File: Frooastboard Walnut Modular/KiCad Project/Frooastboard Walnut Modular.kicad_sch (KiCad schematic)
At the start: 89 parts, among them J1 SW Interface, J2 Conn_01x16, J3 Conn_01x06, J4 Conn_01x06, J5 Conn_01x10, J6 Conn_01x12, J7 Conn_01x04, U1 RP2040, U2 SPX3819M5-L-3-3, U3 W25Q32JVZP, U4 nRF8001, U5 IS31FL3733-QF, U6 FS312F-G, U7 FS8205, U8 IP2312, Y1 32.768kHz, Y2 16MHz, Y3 12MHz

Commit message: some backup
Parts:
- BT1: footprint TestPoint:TestPoint_Pad_D1.5mm -> TestPoint:TestPoint_2Pads_Pitch5.08mm_Drill1.3mm
- J1: footprint Connector_PinHeader_2.54mm:PinHeader_1x05_P2.54mm_Vertical -> Connector_PinHeader_1.27mm:PinHeader_1x05_P1.27mm_Vertical
- TP5: footprint TestPoint:TestPoint_Pad_D1.5mm -> Connector_PinHeader_1.27mm:PinHeader_1x02_P1.27mm_Vertical
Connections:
- net RP_RESET: now also R8.2, U1.26 (~{RUN})
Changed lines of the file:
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@@
   (junction (at 255.27 182.88) (diameter 0) (color 0 0 0 0)
   )
+  (junction (at 30.48 34.29) (diameter 0) (color 0 0 0 0)
+  )
   (junction (at 309.245 184.15) (diameter 0) (color 0 0 0 0)
   )
@@
     (stroke (width 0) (type default) (color 0 0 0 0))
   )
+  (wire (pts (xy 27.94 34.29) (xy 30.48 34.29))
+    (stroke (width 0) (type default) (color 0 0 0 0))
+  )
   (wire (pts (xy 370.84 107.95) (xy 370.84 110.49))
     (stroke (width 0) (type default) (color 0 0 0 0))
@@
     )
   )
+  (global_label "RP_RESET" (shape input) (at 27.94 34.29 180) (fields_autoplaced)
+    (effects (font (size 1.27 1.27)) (justify right))
+    (property "Intersheet References" "${INTERSHEET_REFS}" (id 0) (at 16.274 34.2106 0)
+      (effects (font (size 1.27 1.27)) (justify right) hide)
+    )
+  )
   (global_label "NRF_REQN" (shape input) (at 76.2 90.17 0) (fields_autoplaced)
     (effects (font (size 1.27 1.27)) (justify left))
@@
       (effects (font (size 1.27 1.27)) (justify left))
     )
-    (property "Footprint" "TestPoint:TestPoint_Pad_D1.5mm" (id 2) (at 294.64 84.836 90)
+    (property "Footprint" "TestPoint:TestPoint_2Pads_Pitch5.08mm_Drill1.3mm" (id 2) (at 294.64 84.836 90)
       (effects (font (size 1.27 1.27)) hide)
     )
@@
       (effects (font (size 1.27 1.27)) (justify right))
     )
-    (property "Footprint" "Connector_PinHeader_2.54mm:PinHeader_1x05_P2.54mm_Vertical" (id 2) (at 177.8 107.95 0)
+    (property "Footprint" "Connector_PinHeader_1.27mm:PinHeader_1x05_P1.27mm_Vertical" (id 2) (at 177.8 107.95 0)
       (effects (font (size 1.27 1.27)) hide)
     )
@@
     (property "Reference" "TP5" (id 0) (at 153.67 30.48 0))
     (property "Value" "QSPI_CS" (id 1) (at 153.67 33.02 0))
-    (property "Footprint" "TestPoint:TestPoint_Pad_D1.5mm" (id 2) (at 153.67 36.83 0)
+    (property "Footprint" "Connector_PinHeader_1.27mm:PinHeader_1x02_P1.27mm_Vertical" (id 2) (at 153.67 36.83 0)
       (effects (font (size 1.27 1.27)) hide)
     )
@@
     )
     (path "/70bcad84-f74d-4bdd-ae2d-c3166191a925"
-      (reference "BT1") (unit 1) (value "Battery_Cell") (footprint "TestPoint:TestPoint_Pad_D1.5mm")
+      (reference "BT1") (unit 1) (value "Battery_Cell") (footprint "TestPoint:TestPoint_2Pads_Pitch5.08mm_Drill1.3mm")
     )
     (path "/2ca352a4-ce7c-4a8a-bb6f-4e1344993b4f"
@@
     )
     (path "/9151085a-7b41-4963-b313-b0cf7786b5dd"
-      (reference "J1") (unit 1) (value "SW Interface") (footprint "Connector_PinHeader_2.54mm:PinHeader_1x05_P2.54mm_Vertical")
+      (reference "J1") (unit 1) (value "SW Interface") (footprint "Connector_PinHeader_1.27mm:PinHeader_1x05_P1.27mm_Vertical")
     )
     (path "/3b4d4f21-563d-4b4f-a6f8-fd0f3231dd95"
@@
     )
     (path "/b6d4088c-3919-4173-8f2b-bc5f0489b775"
-      (reference "TP5") (unit 1) (value "QSPI_CS") (footprint "TestPoint:TestPoint_Pad_D1.5mm")
+      (reference "TP5") (unit 1) (value "QSPI_CS") (footprint "Connector_PinHeader_1.27mm:PinHeader_1x02_P1.27mm_Vertical")
     )
     (path "/7a332b0c-4cba-438b-85c1-9efe2690fb62"

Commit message: do some stuff (probably redo that)
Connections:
- net ANT1: now also L1.1, L2.1; no longer L2.2, L3.1
- net ANT2: now also L2.2, L3.1; no longer L1.1, L2.1

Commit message: mmmhhh rp2040
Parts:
- removed C27: 100n, Capacitor_SMD:C_0805_2012Metric, symbol Device:C_Small
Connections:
- net QSPI_CS: no longer R9.1, TP5.2
- net DP: now reaches J7.3 (Pin_3), R23.2
- net DN: now reaches J7.4 (Pin_4), R24.2
- new net QSPI_CS_TP: R9.1, TP5.2
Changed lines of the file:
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@@
   (junction (at 384.81 54.61) (diameter 0) (color 0 0 0 0)
   )
-  (junction (at 186.69 74.93) (diameter 0) (color 0 0 0 0)
-  )
   (junction (at 171.45 36.83) (diameter 0) (color 0 0 0 0)
   )
@@
   (junction (at 96.52 243.84) (diameter 0) (color 0 0 0 0)
   )
-  (junction (at 186.69 85.09) (diameter 0) (color 0 0 0 0)
-  )
   (junction (at 59.69 257.81) (diameter 0) (color 0 0 0 0)
   )
@@
     (stroke (width 0) (type default) (color 0 0 0 0))
   )
-  (wire (pts (xy 194.31 85.09) (xy 194.31 82.55))
-    (stroke (width 0) (type default) (color 0 0 0 0))
-  )
   (wire (pts (xy 146.05 36.83) (xy 146.05 39.37))
     (stroke (width 0) (type default) (color 0 0 0 0))
@@
     (stroke (width 0) (type default) (color 0 0 0 0))
   )
-  (wire (pts (xy 194.31 74.93) (xy 186.69 74.93))
-    (stroke (width 0) (type default) (color 0 0 0 0))
-  )
   (wire (pts (xy 275.59 93.98) (xy 280.67 93.98))
     (stroke (width 0) (type default) (color 0 0 0 0))
@@
     (stroke (width 0) (type default) (color 0 0 0 0))
   )
-  (wire (pts (xy 194.31 77.47) (xy 194.31 74.93))
-    (stroke (width 0) (type default) (color 0 0 0 0))
-  )
   (wire (pts (xy 280.67 73.66) (xy 275.59 73.66))
     (stroke (width 0) (type default) (color 0 0 0 0))
@@
     (stroke (width 0) (type default) (color 0 0 0 0))
   )
-  (wire (pts (xy 186.69 85.09) (xy 194.31 85.09))
-    (stroke (width 0) (type default) (color 0 0 0 0))
-  )
   (wire (pts (xy 163.83 207.01) (xy 163.83 209.55))
     (stroke (width 0) (type default) (color 0 0 0 0))
@@
     (effects (font (size 1.27 1.27)) (justify left bottom))
   )
-  (label "QSPI_CS" (at 158.75 36.83 0)
+  (label "QSPI_CS_TP" (at 158.75 36.83 0)
+    (effects (font (size 1.27 1.27)) (justify left bottom))
+  )
+  (label "DP" (at 168.91 130.81 0)
+    (effects (font (size 1.27 1.27)) (justify left bottom))
+  )
+  (label "DN" (at 168.91 133.35 0)
     (effects (font (size 1.27 1.27)) (justify left bottom))
   )
@@
     (pin "2")
   )
-  (symbol (lib_id "Device:C_Small") (at 194.31 80.01 0) (unit 1)
-    (in_bom yes) (on_board yes) (fields_autoplaced)
-    (property "Reference" "C27" (id 0) (at 196.85 78.7462 0)
-      (effects (font (size 1.27 1.27)) (justify left))
-    )
-    (property "Value" "100n" (id 1) (at 196.85 81.2862 0)
-      (effects (font (size 1.27 1.27)) (justify left))
-    )
-    (property "Footprint" "Capacitor_SMD:C_0805_2012Metric" (id 2) (at 194.31 80.01 0)
-      (effects (font (size 1.27 1.27)) hide)
-    )
-    (property "Datasheet" "~" (id 3) (at 194.31 80.01 0)
-      (effects (font (size 1.27 1.27)) hide)
-    )
-    (pin "1")
-    (pin "2")
-  )
   (symbol (lib_id "power:+1V1") (at 204.47 72.39 0) (unit 1)
     (in_bom yes) (on_board yes) (fields_autoplaced)
@@
       (reference "C26") (unit 1) (value "100n") (footprint "Capacitor_SMD:C_0805_2012Metric")
     )
-    (path "/de514b0b-e2c1-4cdd-873b-610f95c72aa7"
-      (reference "C27") (unit 1) (value "100n") (footprint "Capacitor_SMD:C_0805_2012Metric")
-    )
     (path "/e14c0760-6866-454a-bf39-e495fbf1ff41"

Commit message: stuff
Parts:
- removed BT1: Battery_Cell, TestPoint:TestPoint_2Pads_Pitch5.08mm_Drill1.3mm, symbol Device:Battery_Cell
- removed C1, C2, C4: 100n, Capacitor_SMD:C_0402_1005Metric, symbol Device:C_Small
- removed C10, C11: 12p, Capacitor_SMD:C_0402_1005Metric, symbol Device:C_Small
- removed C12: 1.8p, Capacitor_SMD:C_0402_1005Metric, symbol Device:C_Small
- removed C13: 1.2p, Capacitor_SMD:C_0402_1005Metric, symbol Device:C_Small
- removed C29: 10n, Capacitor_SMD:C_0805_2012Metric, symbol Device:C_Small
- removed C3: 1n, Capacitor_SMD:C_0402_1005Metric, symbol Device:C_Small
- removed C30, C36: 22u, Capacitor_SMD:C_0805_2012Metric, symbol Device:C
- removed C31: 10u, Capacitor_SMD:C_0805_2012Metric, symbol Device:C_Small
- removed C32: 100n, Capacitor_SMD:C_0805_2012Metric, symbol Device:C_Small
- removed C37: 10u, Capacitor_SMD:C_0805_2012Metric, symbol Device:C
- removed C5: 33n, Capacitor_SMD:C_0402_1005Metric, symbol Device:C_Small
- removed C6, C7: 15p, Capacitor_SMD:C_0402_1005Metric, symbol Device:C_Small
- removed C8: 2.2n, Capacitor_SMD:C_0402_1005Metric, symbol Device:C_Small
- removed C9: Not Mounted, Capacitor_SMD:C_0402_1005Metric, symbol Device:C_Small
- removed D1: GREEN, LED_SMD:LED_0805_2012Metric, symbol Device:LED
- removed D2: RED, LED_SMD:LED_0805_2012Metric, symbol Device:LED
- removed L1: 5.6nH, Inductor_SMD:L_0402_1005Metric, symbol Device:L_Small
- removed L2: 8.2nH, Inductor_SMD:L_0402_1005Metric, symbol Device:L_Small
- removed L3: 3.9nH, Inductor_SMD:L_0402_1005Metric, symbol Device:L_Small
- removed L4: 1uH, Inductor_SMD:L_6.3x6.3_H3, symbol Device:L
- removed R1: 10k, Resistor_SMD:R_0805_2012Metric, symbol Device:R_Small
- removed R10: 2k, Resistor_SMD:R_0805_2012Metric, symbol Device:R
- removed R12: 0k5, Resistor_SMD:R_0805_2012Metric, symbol Device:R
- removed R13, R14: 1M, Resistor_SMD:R_0805_2012Metric, symbol Device:R_Small
- removed R15, R16: 0k1, Resistor_SMD:R_0805_2012Metric, symbol Device:R
- removed R17, R20: NC, Resistor_SMD:R_0805_2012Metric, symbol Device:R
- removed R18: 51k, Resistor_SMD:R_0805_2012Metric, symbol Device:R
- removed R19: 1k, Resistor_SMD:R_0805_2012Metric, symbol Device:R
- removed R2: 22k, Resistor_SMD:R_0805_2012Metric, symbol Device:R_Small
- removed TP1: NRF_TXD, TestPoint:TestPoint_Pad_D1.5mm, symbol Connector:TestPoint
- removed TP2: NRF_RXD, TestPoint:TestPoint_Pad_D1.5mm, symbol Connector:TestPoint
- removed TP3: NRF_RESET, TestPoint:TestPoint_Pad_D1.5mm, symbol Connector:TestPoint
- removed TP4: NRF_IREF, TestPoint:TestPoint_Pad_D1.5mm, symbol Connector:TestPoint
- removed U2: SPX3819M5-L-3-3, Package_TO_SOT_SMD:SOT-23-5, symbol Regulator_Linear:SPX3819M5-L-3-3
- removed U4: nRF8001, Package_DFN_QFN:QFN-32-1EP_5x5mm_P0.5mm_EP3.45x3.45mm, symbol RF_Bluetooth:nRF8001
- removed U6: FS312F-G, Package_TO_SOT_SMD:SOT-23-6, symbol Frooastboard Symbols:FS312F-G
- removed U7: FS8205, Package_TO_SOT_SMD:SOT-23-6, symbol Frooastboard Symbols:FS8205
- removed U8: IP2312, Package_SO:SOIC-8-1EP_3.9x4.9mm_P1.27mm_EP2.41x3.3mm, symbol Frooastboard Symbols:IP2312
- removed Y1: 32.768kHz, Crystal:Crystal_SMD_EuroQuartz_EQ161-2Pin_3.2x1.5mm, symbol Device:Crystal_Small
- removed Y2: 16MHz, Crystal:Crystal_SMD_3225-4Pin_3.2x2.5mm, symbol Device:Crystal_GND24_Small
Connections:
- no-connect marks 6 -> 3
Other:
- note removed: "NC for 2.1A"
- note removed: "NC for 4.2V"
- moved on the sheet: C28, C33, C34, C35, J2, J3, J4, R11, R6, R7, U5

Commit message: change some stuff maybe finally get started
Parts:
- removed C14, C15: 22p, Capacitor_SMD:C_0805_2012Metric, symbol Device:C_Small
- removed C16, C17, C33: 10u, Capacitor_SMD:C_0805_2012Metric, symbol Device:C_Small
- removed C18, C19, C20, C21, C22, C23, C24, C25, C26: 100n, Capacitor_SMD:C_0805_2012Metric, symbol Device:C_Small
- removed C28: 0.1u, Capacitor_SMD:C_0805_2012Metric, symbol Device:C_Small
- removed C34, C35: 10u, Capacitor_Tantalum_SMD:CP_EIA-2012-15_AVX-P, symbol Device:C_Polarized
- removed J1: SW Interface, Connector_PinHeader_1.27mm:PinHeader_1x05_P1.27mm_Vertical, symbol Connector:Conn_01x05_Male
- removed J2: Conn_01x16, Frooastboard Footprints:PinHeader_1x16_P1.27mm_Vertical, symbol Connector_Generic:Conn_01x16
- removed J3, J4: Conn_01x06, Frooastboard Footprints:PinHeader_1x06_P1.27mm_Vertical, symbol Connector_Generic:Conn_01x06
- removed J5: Conn_01x10, Frooastboard Footprints:PinHeader_1x10_P1.27mm_Vertical, symbol Connector_Generic:Conn_01x10
- removed J6: Conn_01x12, Frooastboard Footprints:PinHeader_1x12_P1.27mm_Vertical, symbol Connector_Generic:Conn_01x12
- removed J7: Conn_01x04, Frooastboard Footprints:PinHeader_1x04_P1.27mm_Vertical, symbol Connector_Generic:Conn_01x04
- removed R11, R7: 100k, Resistor_SMD:R_0805_2012Metric, symbol Device:R
- removed R23, R24: 27R, Resistor_SMD:R_0805_2012Metric, symbol Device:R_Small
- removed R3, R9: 1k, Resistor_SMD:R_0805_2012Metric, symbol Device:R_Small
- removed R4, R5: 2k, Resistor_SMD:R_0805_2012Metric, symbol Device:R_Small
- removed R6: 20k, Resistor_SMD:R_0805_2012Metric, symbol Device:R
- removed R8: 10k, Resistor_SMD:R_0805_2012Metric, symbol Device:R_Small
- removed TP5: QSPI_CS, Connector_PinHeader_1.27mm:PinHeader_1x02_P1.27mm_Vertical, symbol Connector:TestPoint_2Pole
- removed U1: RP2040, Frooastboard Footprints:RP2040-QFN-56, symbol Frooastboard Symbols:RP2040
- removed U3: W25Q32JVZP, Package_SON:WSON-8-1EP_6x5mm_P1.27mm_EP3.4x4.3mm, symbol Memory_Flash:W25Q32JVZP
- removed U5: IS31FL3733-QF, Package_DFN_QFN:QFN-48-1EP_6x6mm_P0.4mm_EP4.2x4.2mm, symbol Driver_LED:IS31FL3733-QF
- removed Y3: 12MHz, Crystal:Crystal_SMD_3225-4Pin_3.2x2.5mm, symbol Device:Crystal_GND24_Small
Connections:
- no-connect marks 3 -> 0
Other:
- added sheet MM2040 (MM2040.kicad_sch)

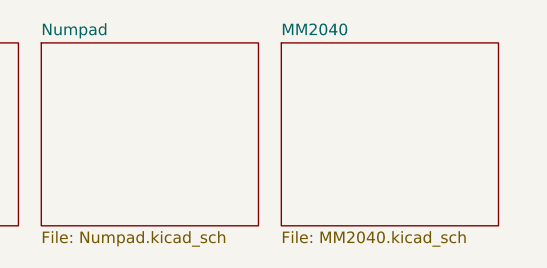
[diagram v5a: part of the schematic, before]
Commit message: import mm2040
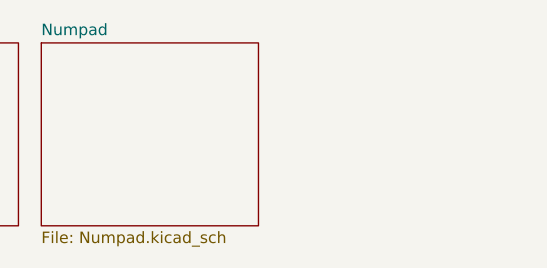
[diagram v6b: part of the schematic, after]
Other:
- removed sheet MM2040
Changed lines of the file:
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@@
-    )
-  )
-  (sheet (at 100.33 20.32) (size 24.13 20.32) (fields_autoplaced)
-    (stroke (width 0.1524) (type solid))
-    (fill (color 0 0 0 0.0000))
-    (property "Sheetname" "MM2040" (at 100.33 19.6084 0)
-      (effects (font (size 1.27 1.27)) (justify left bottom))
-    )
-    (property "Sheetfile" "MM2040.kicad_sch" (at 100.33 41.2246 0)
-      (effects (font (size 1.27 1.27)) (justify left top))
-    )
-    (instances
-      (project "Frooastboard Walnut Modular"
-        (path "/e63e39d7-6ac0-4ffd-8aa3-1841a4541b55" (page "5"))
-      )
     )
   )
